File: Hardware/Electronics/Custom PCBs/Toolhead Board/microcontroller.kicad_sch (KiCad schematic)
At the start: 35 parts, among them J1 USB C Receptacle, J2 Conn_02x08_Odd_Even, J3 Conn_02x08_Odd_Even, J4 Conn_02x08_Odd_Even, J5 Conn_02x04_Odd_Even, J6 Conn_02x04_Odd_Even, SW1 BOOT, SW2 RESET, U3 RP2040, U4 W25Q128JVS, Y1 12MHz/12pF/50Ω/20ppm

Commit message: Update layout
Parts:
- J1: footprint Connector_USB:USB_C_Receptacle_GCT_USB4105-xx-A_16P_TopMnt_Horizontal -> Connector_USB:USB_C_Receptacle_JAE_DX07S016JA1R1500
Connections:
- net TH0 is gone; now on net THERM0: U3.34 (GPIO22)
- net TH1 is gone; now on net THERM1: U3.35 (GPIO23)
- net TH2 is gone; now on net THERM2: U3.36 (GPIO24)
- net TH3 is gone; now on net THERM3: U3.37 (GPIO25)
- net +24V: now also J3.5 (Pin_5)
- net CAN_RX: no longer J3.7 (Pin_7)
- net CAN_S: no longer J3.9 (Pin_9)
- net CAN_TX: no longer J3.5 (Pin_5)
- new net CAN_H: J3.7 (Pin_7)
- new net CAN_L: J3.9 (Pin_9)
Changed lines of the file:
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@@
 	)
 	(junction
+		(at 59.69 147.32)
+		(diameter 0)
+		(color 0 0 0 0)
+	)
+	(junction
 		(at 104.14 162.56)
 		(diameter 0)
@@
 	(wire
 		(pts
+			(xy 59.69 147.32) (xy 59.69 149.86)
+		)
+		(stroke
+			(width 0)
+			(type default)
+		)
+	)
+	(wire
+		(pts
 			(xy 93.98 31.75) (xy 96.52 31.75)
 		)
@@
 		)
 	)
+	(global_label "THERM0"
+		(shape input)
+		(at 109.22 97.79 0)
+		(fields_autoplaced yes)
+		(effects
+			(font
+				(size 1.27 1.27)
+			)
+			(justify left)
+		)
+		(property "Intersheetrefs" "${INTERSHEET_REFS}"
+			(at 119.5832 97.79 0)
+			(effects
+				(font
+					(size 1.27 1.27)
+				)
+				(justify left)
+				(hide yes)
+			)
+		)
+	)
 	(global_label "24V_PWM2"
 		(shape input)
@@
 		)
 	)
-	(global_label "TH3"
-		(shape input)
-		(at 109.22 105.41 0)
-		(fields_autoplaced yes)
-		(effects
-			(font
-				(size 1.27 1.27)
-			)
-			(justify left)
-		)
-		(property "Intersheetrefs" "${INTERSHEET_REFS}"
-			(at 115.7128 105.41 0)
-			(effects
-				(font
-					(size 1.27 1.27)
-				)
-				(justify left)
-				(hide yes)
-			)
-		)
-	)
 	(global_label "OA1"
 		(shape input)
@@
 		)
 	)
-	(global_label "CAN_S"
-		(shape input)
-		(at 59.69 154.94 180)
-		(fields_autoplaced yes)
-		(effects
-			(font
-				(size 1.27 1.27)
-			)
-			(justify right)
-		)
-		(property "Intersheetrefs" "${INTERSHEET_REFS}"
-			(at 50.8386 154.94 0)
-			(effects
-				(font
-					(size 1.27 1.27)
-				)
-				(justify right)
-				(hide yes)
-			)
-		)
-	)
 	(global_label "OA2"
 		(shape input)
@@
 		)
 	)
-	(global_label "TH0"
-		(shape input)
-		(at 109.22 97.79 0)
-		(fields_autoplaced yes)
-		(effects
-			(font
-				(size 1.27 1.27)
-			)
-			(justify left)
-		)
-		(property "Intersheetrefs" "${INTERSHEET_REFS}"
-			(at 115.7128 97.79 0)
-			(effects
-				(font
-					(size 1.27 1.27)
-				)
-				(justify left)
-				(hide yes)
-			)
-		)
-	)
 	(global_label "MOT_UART"
 		(shape input)
@@
 		)
 	)
-	(global_label "CAN_TX"
-		(shape input)
-		(at 59.69 149.86 180)
-		(fields_autoplaced yes)
-		(effects
-			(font
-				(size 1.27 1.27)
-			)
-			(justify right)
-		)
-		(property "Intersheetrefs" "${INTERSHEET_REFS}"
-			(at 49.871 149.86 0)
-			(effects
-				(font
-					(size 1.27 1.27)
-				)
-				(justify right)
-				(hide yes)
-			)
-		)
-	)
 	(global_label "SDA"
 		(shape input)
@@
 		)
 	)
-	(global_label "TH1"
+	(global_label "THERM3"
 		(shape input)
-		(at 109.22 100.33 0)
+		(at 109.22 105.41 0)
 		(fields_autoplaced yes)
 		(effects
@@
 		)
 		(property "Intersheetrefs" "${INTERSHEET_REFS}"
-			(at 115.7128 100.33 0)
+			(at 119.5832 105.41 0)
 			(effects
 				(font
@@
 		)
 	)
+	(global_label "CAN_L"
+		(shape input)
+		(at 59.69 154.94 180)
+		(fields_autoplaced yes)
+		(effects
+			(font
+				(size 1.27 1.27)
+			)
+			(justify right)
+		)
+		(property "Intersheetrefs" "${INTERSHEET_REFS}"
+			(at 51.02 154.94 0)
+			(effects
+				(font
+					(size 1.27 1.27)
+				)
+				(justify right)
+				(hide yes)
+			)
+		)
+	)
+	(global_label "THERM1"
+		(shape input)
+		(at 109.22 100.33 0)
+		(fields_autoplaced yes)
+		(effects
+			(font
+				(size 1.27 1.27)
+			)
+			(justify left)
+		)
+		(property "Intersheetrefs" "${INTERSHEET_REFS}"
+			(at 119.5832 100.33 0)
+			(effects
+				(font
+					(size 1.27 1.27)
+				)
+				(justify left)
+				(hide yes)
+			)
+		)
+	)
 	(global_label "SERVO6"
 		(shape input)
@@
 		)
 	)
-	(global_label "CAN_RX"
+	(global_label "SERVO3"
 		(shape input)
-		(at 59.69 152.4 180)
+		(at 91.44 154.94 180)
 		(fields_autoplaced yes)
 		(effects
@@
 		)
 		(property "Intersheetrefs" "${INTERSHEET_REFS}"
-			(at 49.5686 152.4 0)
+			(at 81.1977 154.94 0)
 			(effects
 				(font
@@
 		)
 	)
-	(global_label "SERVO3"
+	(global_label "D0"
 		(shape input)
-		(at 91.44 154.94 180)
+		(at 109.22 41.91 0)
 		(fields_autoplaced yes)
 		(effects
@@
 				(size 1.27 1.27)
 			)
-			(justify right)
+			(justify left)
 		)
 		(property "Intersheetrefs" "${INTERSHEET_REFS}"
-			(at 81.1977 154.94 0)
+			(at 114.6847 41.91 0)
 			(effects
 				(font
 					(size 1.27 1.27)
 				)
-				(justify right)
+				(justify left)
 				(hide yes)
 			)
 		)
 	)
-	(global_label "D0"
+	(global_label "D11"
 		(shape input)
-		(at 109.22 41.91 0)
+		(at 109.22 69.85 0)
 		(fields_autoplaced yes)
 		(effects
@@
 		)
 		(property "Intersheetrefs" "${INTERSHEET_REFS}"
-			(at 114.6847 41.91 0)
+			(at 115.8942 69.85 0)
 			(effects
 				(font
@@
 		)
 	)
-	(global_label "TH2"
+	(global_label "MOT_STP"
 		(shape input)
-		(at 109.22 102.87 0)
+		(at 109.22 87.63 0)
 		(fields_autoplaced yes)
 		(effects
@@
 		)
 		(property "Intersheetrefs" "${INTERSHEET_REFS}"
-			(at 115.7128 102.87 0)
+			(at 120.3694 87.63 0)
 			(effects
 				(font
@@
 		)
 	)
-	(global_label "D11"
+	(global_label "CAN_H"
 		(shape input)
-		(at 109.22 69.85 0)
+		(at 59.69 152.4 180)
 		(fields_autoplaced yes)
 		(effects
@@
 				(size 1.27 1.27)
 			)
-			(justify left)
+			(justify right)
 		)
 		(property "Intersheetrefs" "${INTERSHEET_REFS}"
-			(at 115.8942 69.85 0)
+			(at 50.7176 152.4 0)
 			(effects
 				(font
 					(size 1.27 1.27)
 				)
-				(justify left)
+				(justify right)
 				(hide yes)
 			)
 		)
 	)
-	(global_label "MOT_STP"
+	(global_label "THERM2"
 		(shape input)
-		(at 109.22 87.63 0)
+		(at 109.22 102.87 0)
 		(fields_autoplaced yes)
 		(effects
@@
 		)
 		(property "Intersheetrefs" "${INTERSHEET_REFS}"
-			(at 120.3694 87.63 0)
+			(at 119.5832 102.87 0)
 			(effects
 				(font
@@
 			)
 		)
-		(property "Footprint" "Connector_USB:USB_C_Receptacle_GCT_USB4105-xx-A_16P_TopMnt_Horizontal"
+		(property "Footprint" "Connector_USB:USB_C_Receptacle_JAE_DX07S016JA1R1500"
 			(at 208.28 134.62 0)
 			(effects

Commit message: Update toolhead board yet again
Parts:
- renumbered J5 to J2, J2 to J3, J3 to J4, J4 to J5

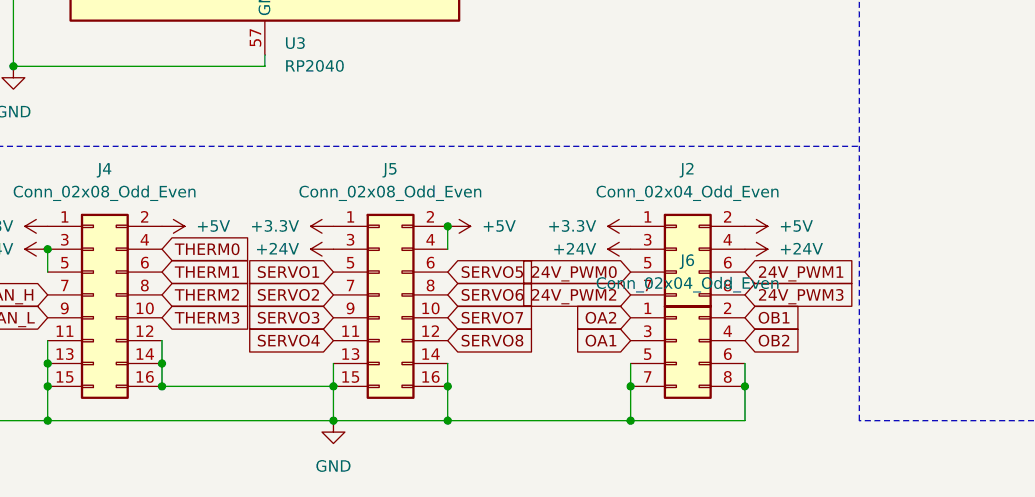
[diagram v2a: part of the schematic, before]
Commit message: Begin replacing CAN transceiver
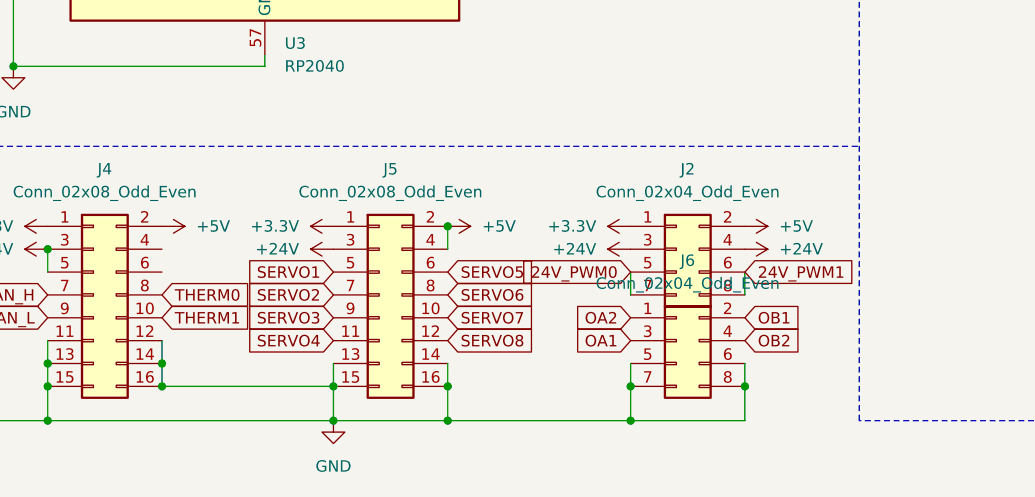
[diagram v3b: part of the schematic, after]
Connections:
- net 24V_PWM2 is gone; now on net 24V_PWM0: J2.7 (Pin_7)
- net 24V_PWM3 is gone; now on net 24V_PWM1: J2.8 (Pin_8)
- net THERM0: now also J4.8 (Pin_8); no longer J4.4 (Pin_4)
- net THERM1: now also J4.10 (Pin_10); no longer J4.6 (Pin_6)
- net THERM2: no longer J4.8 (Pin_8)
- net THERM3: no longer J4.10 (Pin_10)

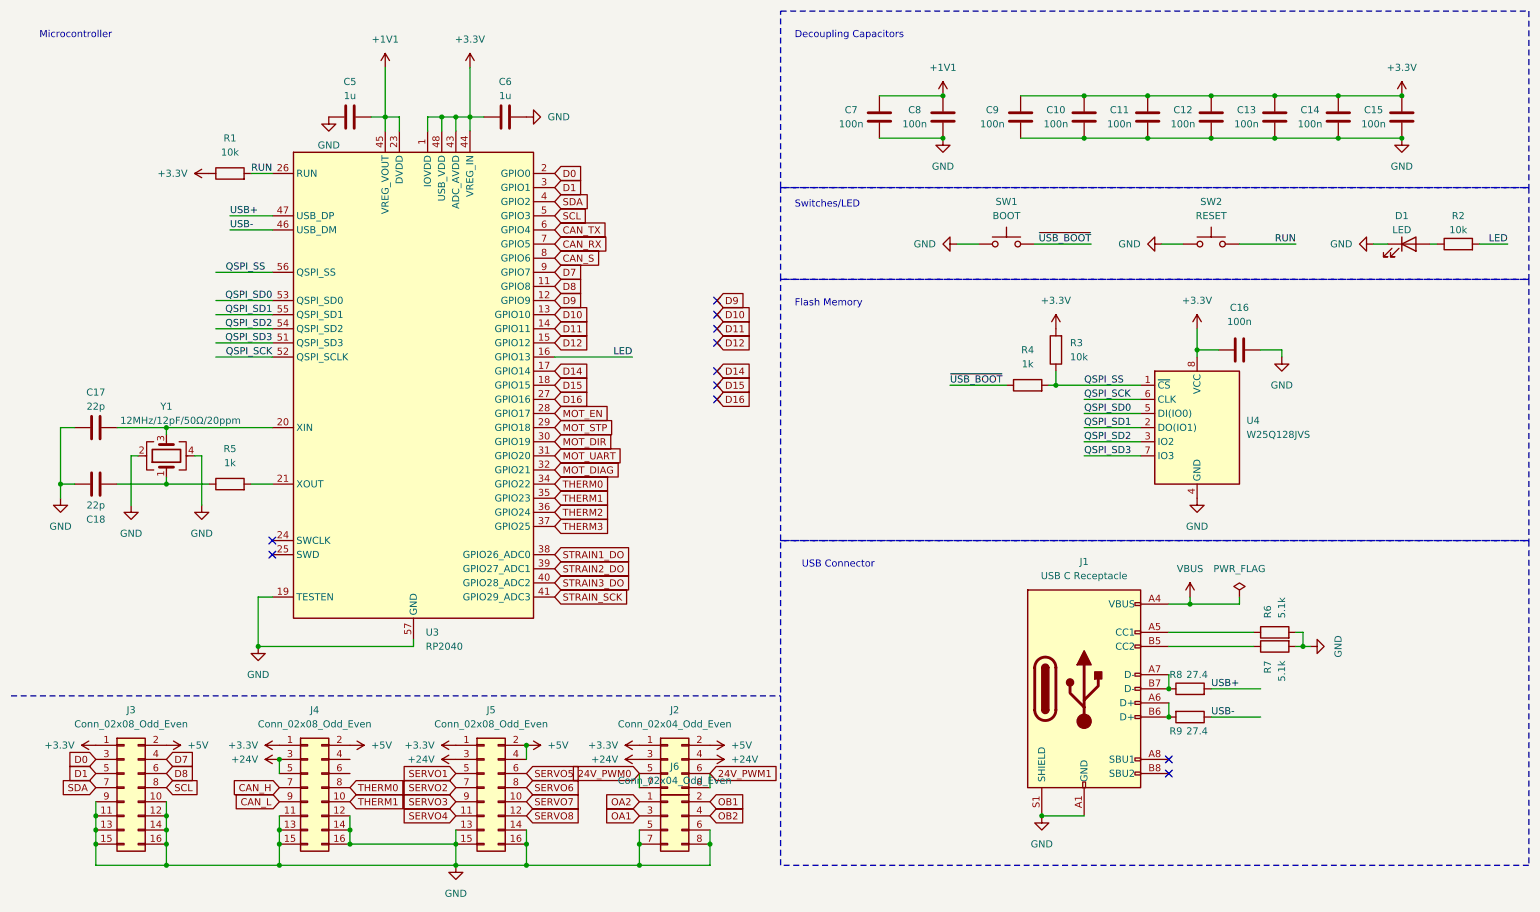
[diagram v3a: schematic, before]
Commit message: Update toolhead schematic+layout and add tolerances to base
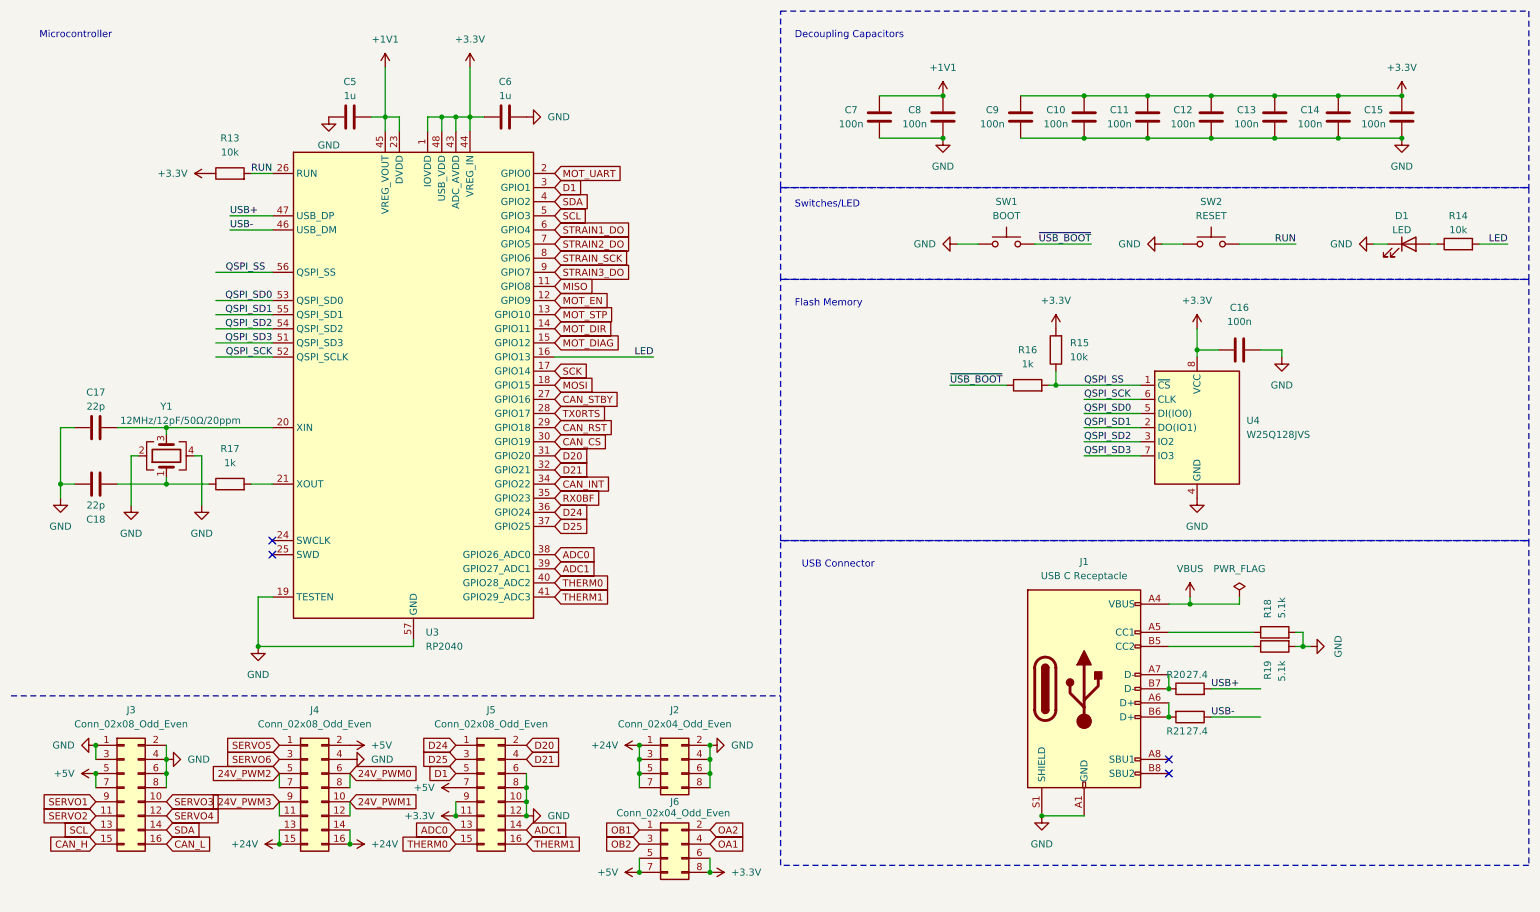
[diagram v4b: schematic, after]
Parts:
- renumbered R1 to R13, R2 to R14, R3 to R15, R4 to R16, R5 to R17, R6 to R18, R7 to R19, R8 to R20, R9 to R21
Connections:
- net CAN_RX is gone; now on net STRAIN2_DO: U3.7 (GPIO5)
- net CAN_S is gone; now on net STRAIN_SCK: U3.8 (GPIO6)
- net CAN_TX is gone; now on net STRAIN1_DO: U3.6 (GPIO4)
- net D10 is gone; now on net MOT_STP: U3.13 (GPIO10)
- net D11 is gone; now on net MOT_DIR: U3.14 (GPIO11)
- net D12 is gone; now on net MOT_DIAG: U3.15 (GPIO12)
- net D9 is gone; now on net MOT_EN: U3.12 (GPIO9)
- net SERVO7 is gone; now on net GND: J5.10 (Pin_10)
- net SERVO8 is gone; now on net GND: J5.12 (Pin_12)
- net +24V: now also J2.1 (Pin_1), J2.5 (Pin_5), J2.7 (Pin_7), J4.13 (Pin_13), J4.14 (Pin_14), J4.15 (Pin_15), J4.16 (Pin_16); no longer J2.4 (Pin_4), J4.3 (Pin_3), J4.5 (Pin_5), J5.3 (Pin_3)
- net +3.3V: now also J5.11 (Pin_11), J5.9 (Pin_9), J6.6 (Pin_6), J6.8 (Pin_8); no longer J2.1 (Pin_1), J3.1 (Pin_1), J4.1 (Pin_1), J5.1 (Pin_1)
- net +5V: now also J3.5 (Pin_5), J3.7 (Pin_7), J5.7 (Pin_7), J6.5 (Pin_5), J6.7 (Pin_7); no longer J2.2 (Pin_2), J3.2 (Pin_2), J5.2 (Pin_2), J5.4 (Pin_4)
- net 24V_PWM0: now also J4.6 (Pin_6), J4.8 (Pin_8); no longer J2.5 (Pin_5), J2.7 (Pin_7)
- net 24V_PWM1: now also J4.10 (Pin_10), J4.12 (Pin_12); no longer J2.6 (Pin_6), J2.8 (Pin_8)
- net CAN_H: now also J3.15 (Pin_15); no longer J4.7 (Pin_7)
- net CAN_L: now also J3.16 (Pin_16); no longer J4.9 (Pin_9)
- net D1: now also J5.5 (Pin_5); no longer J3.5 (Pin_5)
- net GND: now also J2.2 (Pin_2), J2.4 (Pin_4), J2.6 (Pin_6), J2.8 (Pin_8), J3.1 (Pin_1), J3.2 (Pin_2), J3.3 (Pin_3), J3.4 (Pin_4), J3.6 (Pin_6), J3.8 (Pin_8), J4.4 (Pin_4), J5.6 (Pin_6), J5.8 (Pin_8); no longer J3.10 (Pin_10), J3.11 (Pin_11), J3.12 (Pin_12), J3.13 (Pin_13), J3.14 (Pin_14), J3.15 (Pin_15), J3.16 (Pin_16), J3.9 (Pin_9), J4.11 (Pin_11), J4.12 (Pin_12), J4.13 (Pin_13), J4.14 (Pin_14), J4.15 (Pin_15), J4.16 (Pin_16), J5.13 (Pin_13), J5.14 (Pin_14), J5.15 (Pin_15), J5.16 (Pin_16), J6.5 (Pin_5), J6.6 (Pin_6), J6.7 (Pin_7), J6.8 (Pin_8)
- net MOT_DIAG: no longer U3.32 (GPIO21)
- net MOT_DIR: no longer U3.30 (GPIO19)
- net MOT_EN: no longer U3.28 (GPIO17)
- net MOT_STP: no longer U3.29 (GPIO18)
- net MOT_UART: now also U3.2 (GPIO0); no longer U3.31 (GPIO20)
- net OA1: now also J6.4 (Pin_4); no longer J6.3 (Pin_3)
- net OA2: now also J6.2 (Pin_2); no longer J6.1 (Pin_1)
- net OB1: now also J6.1 (Pin_1); no longer J6.2 (Pin_2)
- net OB2: now also J6.3 (Pin_3); no longer J6.4 (Pin_4)
- net SCL: now also J3.13 (Pin_13); no longer J3.8 (Pin_8)
- net SDA: now also J3.14 (Pin_14); no longer J3.7 (Pin_7)
- net SERVO1: now also J3.9 (Pin_9); no longer J5.5 (Pin_5)
- net SERVO2: now also J3.11 (Pin_11); no longer J5.7 (Pin_7)
- net SERVO3: now also J3.10 (Pin_10); no longer J5.9 (Pin_9)
- net SERVO4: now also J3.12 (Pin_12); no longer J5.11 (Pin_11)
- net SERVO5: now also J4.1 (Pin_1); no longer J5.6 (Pin_6)
- net SERVO6: now also J4.3 (Pin_3); no longer J5.8 (Pin_8)
- net STRAIN1_DO: no longer U3.38 (GPIO26_ADC0)
- net STRAIN2_DO: no longer U3.39 (GPIO27_ADC1)
- net STRAIN3_DO: now also U3.9 (GPIO7); no longer U3.40 (GPIO28_ADC2)
- net STRAIN_SCK: no longer U3.41 (GPIO29_ADC3)
- net THERM0: now also J5.15 (Pin_15), U3.40 (GPIO28_ADC2); no longer J4.8 (Pin_8), U3.34 (GPIO22)
- net THERM1: now also J5.16 (Pin_16), U3.41 (GPIO29_ADC3); no longer J4.10 (Pin_10), U3.35 (GPIO23)
- removed net D0: J3.3 (Pin_3), U3.2 (GPIO0)
- net D14 renamed SCK
- net D15 renamed MOSI
- net D16 renamed CAN_STBY
- removed net D7: J3.4 (Pin_4), U3.9 (GPIO7)
- net D8 renamed MISO
- net MISO: no longer J3.6 (Pin_6)
- net THERM2 renamed D24
- net D24: now also J5.1 (Pin_1)
- net THERM3 renamed D25
- net D25: now also J5.3 (Pin_3)
- new net 24V_PWM2: J4.5 (Pin_5), J4.7 (Pin_7)
- new net 24V_PWM3: J4.11 (Pin_11), J4.9 (Pin_9)
- new net ADC0: J5.13 (Pin_13), U3.38 (GPIO26_ADC0)
- new net ADC1: J5.14 (Pin_14), U3.39 (GPIO27_ADC1)
- new net CAN_CS: U3.30 (GPIO19)
- new net CAN_INT: U3.34 (GPIO22)
- new net CAN_RST: U3.29 (GPIO18)
- new net D20: J5.2 (Pin_2), U3.31 (GPIO20)
- new net D21: J5.4 (Pin_4), U3.32 (GPIO21)
- new net RX0BF: U3.35 (GPIO23)
- new net TX0RTS: U3.28 (GPIO17)
- no-connect marks 11 -> 4
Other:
- moved on the sheet: J6

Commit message: Update layout
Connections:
- net +3.3V: now also J5.13 (Pin_13); no longer J5.9 (Pin_9)
- net +5V: now also J5.9 (Pin_9); no longer J5.7 (Pin_7)
- net ADC0: now also J5.2 (Pin_2); no longer J5.13 (Pin_13)
- net ADC1: now also J5.3 (Pin_3); no longer J5.14 (Pin_14)
- net CAN_H: now also J3.16 (Pin_16); no longer J3.15 (Pin_15)
- net CAN_L: now also J3.15 (Pin_15); no longer J3.16 (Pin_16)
- net D1: now also J3.9 (Pin_9); no longer J5.5 (Pin_5)
- net D20: now also J3.10 (Pin_10); no longer J5.2 (Pin_2)
- net D21: now also J3.11 (Pin_11); no longer J5.4 (Pin_4)
- net D24: now also J3.12 (Pin_12); no longer J5.1 (Pin_1)
- net D25: now also J5.1 (Pin_1); no longer J5.3 (Pin_3)
- net GND: now also J5.14 (Pin_14); no longer J5.6 (Pin_6)
- net SERVO1: now also J4.1 (Pin_1); no longer J3.9 (Pin_9)
- net SERVO2: now also J4.3 (Pin_3); no longer J3.11 (Pin_11)
- net SERVO3: now also J5.5 (Pin_5); no longer J3.10 (Pin_10)
- net SERVO4: now also J5.4 (Pin_4); no longer J3.12 (Pin_12)
- net SERVO5: now also J5.7 (Pin_7); no longer J4.1 (Pin_1)
- net SERVO6: now also J5.6 (Pin_6); no longer J4.3 (Pin_3)

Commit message: Update layout
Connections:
- net +5V: now also J5.7 (Pin_7)
- net ADC1: now also J5.1 (Pin_1); no longer J5.3 (Pin_3)
- net D25: no longer J5.1 (Pin_1)
- net SERVO3: now also J5.3 (Pin_3); no longer J5.5 (Pin_5)
- net SERVO5: now also J5.5 (Pin_5); no longer J5.7 (Pin_7)

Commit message: one damn unconnected item
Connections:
- no-connect marks 4 -> 5
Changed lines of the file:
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@@
+	)
+	(no_connect
+		(at 137.16 106.68)
 	)
 	(no_connect
@@
 			(effects
 				(font
+					(size 1.27 1.27)
+				)
+				(justify left)
+				(hide yes)
+			)
+		)
+	)
+	(global_label "D25"
+		(shape input)
+		(at 137.16 106.68 0)
+		(fields_autoplaced yes)
+		(effects
+			(font
+				(size 1.27 1.27)
+			)
+			(justify left)
+		)
+		(property "Intersheetrefs" "${INTERSHEET_REFS}"
+			(at 143.8342 106.68 0)
+			(effects
+				(font
